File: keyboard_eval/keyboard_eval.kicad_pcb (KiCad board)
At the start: 2 copper layers, 3.4 x 3 mm, 65 parts, among them IC1 IS31FL3733B-TQLS4, J1 Conn_01x03, J2 Conn_01x04, J3 Conn_01x04, J4 Conn_01x07, J5 Conn_01x03, J6 Conn_01x03, J7 Conn_01x06, SW1 RotaryEncoder_Switch

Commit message: WIP layout
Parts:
- added JP4: Jumper_2_Open, Jumper:SolderJumper-2_P1.3mm_Open_RoundedPad1.0x1.5mm, B.Cu at (59.9, 24.1)
- C10, C11, C12, C9, JP1, R5: moved to B.Cu
- JP2, JP3: value Jumper_3_Open -> Jumper_2_Open; footprint Jumper:SolderJumper-3_P1.3mm_Open_RoundedPad1.0x1.5mm -> Jumper:SolderJumper-2_P1.3mm_Open_RoundedPad1.0x1.5mm; moved to B.Cu
- moved R2 193.0 mm to (49.9, 26.2), turned to 180 degrees
- moved C3 192.1 mm to (46.4, 28.2), turned to 180 degrees
- moved C7 190.4 mm to (51.0, 36.5), turned to -90 degrees
- moved C8 185.5 mm to (49.2, 36.5), turned to -90 degrees
- moved C4 185.4 mm to (46.4, 29.9), turned to 180 degrees
- moved R1 176.7 mm to (49.9, 24.2), turned to 180 degrees
- moved R5 175.7 mm to (45.0, 31.4), turned to -90 degrees
- moved R3 175.4 mm to (53.6, 26.2), turned to 180 degrees
- moved JP3 173.9 mm to (46.3, 24.6)
- moved R4 173.0 mm to (56.1, 28.9)
- moved JP2 171.4 mm to (42.6, 24.6)
- moved J3 170.5 mm to (53.2, 21.1), turned to -90 degrees
- moved C6 168.3 mm to (46.4, 33.6), turned to 180 degrees
- moved JP1 167.0 mm to (72.3, 27.7), turned to 90 degrees
- moved C2 165.4 mm to (50.3, 28.1)
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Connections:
- J3 pad 3: Net-(J3-Pad3) -> OLED_SCL
- J3 pad 4: Net-(J3-Pad4) -> OLED_SDA
- JP2 pad 1: OLED_SDA -> LED_SCL
- JP2 pad 2: LED_SDA -> OLED_SDA
- JP3 pad 1: OLED_SCL -> LED_SDA
- JP3 pad 2: LED_SCL -> OLED_SCL
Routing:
- net Col0: track 0.00 -> 102.8 mm, vias 0 -> 7
- net Col2: track 0.00 -> 90.4 mm, vias 0 -> 3
- net Col1: track 0.00 -> 83.0 mm, vias 0 -> 5
- net Row_RE: track 0.00 -> 75.7 mm, vias 0 -> 1
- net Row0: track 0.00 -> 72.8 mm
- net Net-(D11-Pad2): track 0.00 -> 61.4 mm, vias 0 -> 2
- net Net-(D12-Pad2): track 0.00 -> 60.4 mm
- net Row1: track 0.00 -> 53.9 mm
- net Net-(D13-Pad2): track 0.00 -> 53.1 mm
- net Row2_G: track 0.00 -> 51.3 mm, vias 0 -> 4
- net Row2: track 0.00 -> 48.6 mm, vias 0 -> 1
- net Row1_G: track 0.00 -> 44.5 mm, vias 0 -> 4
- net Row0_G: track 0.00 -> 44.2 mm, vias 0 -> 4
- net Row0_R: track 0.00 -> 41.2 mm
- net Row0_B: track 0.00 -> 40.9 mm
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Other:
- board size 3.4 x 3 mm -> 66.5 x 83.5 mm

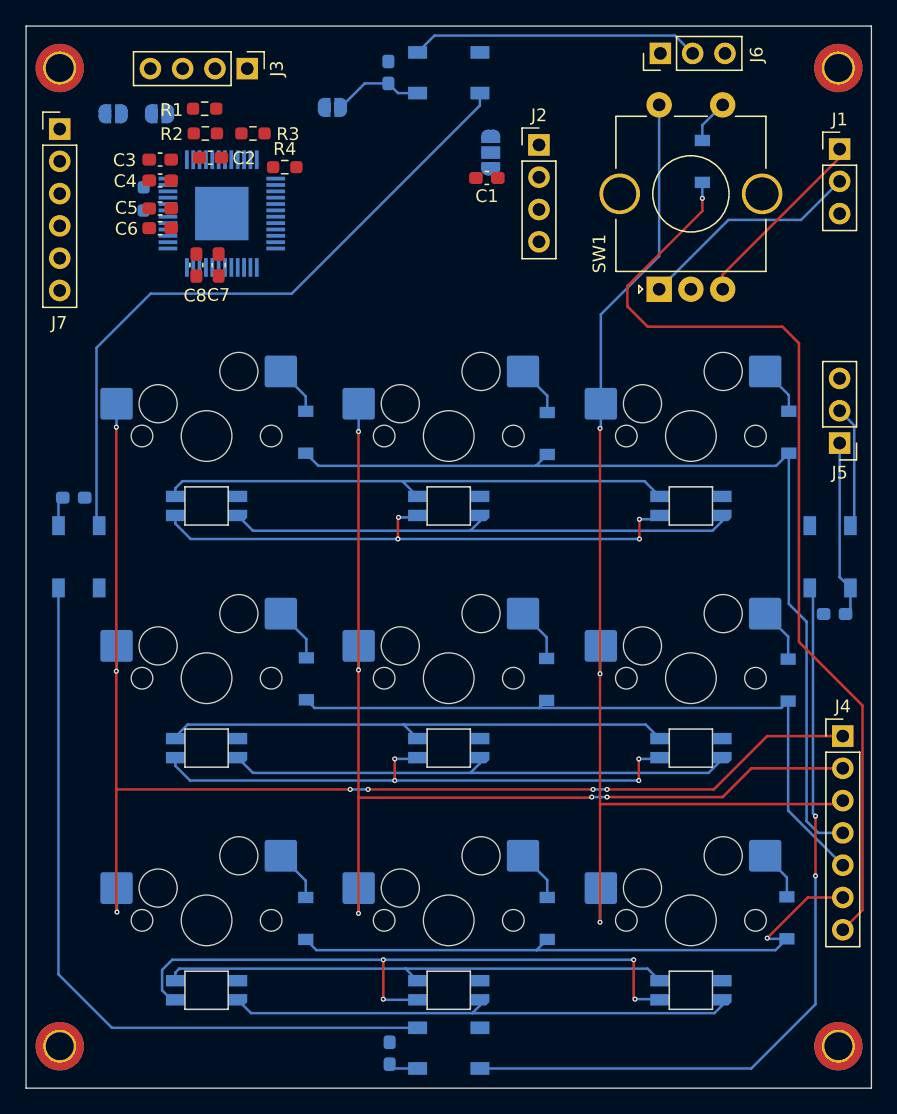
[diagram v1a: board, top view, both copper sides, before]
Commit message: Finished initial layout
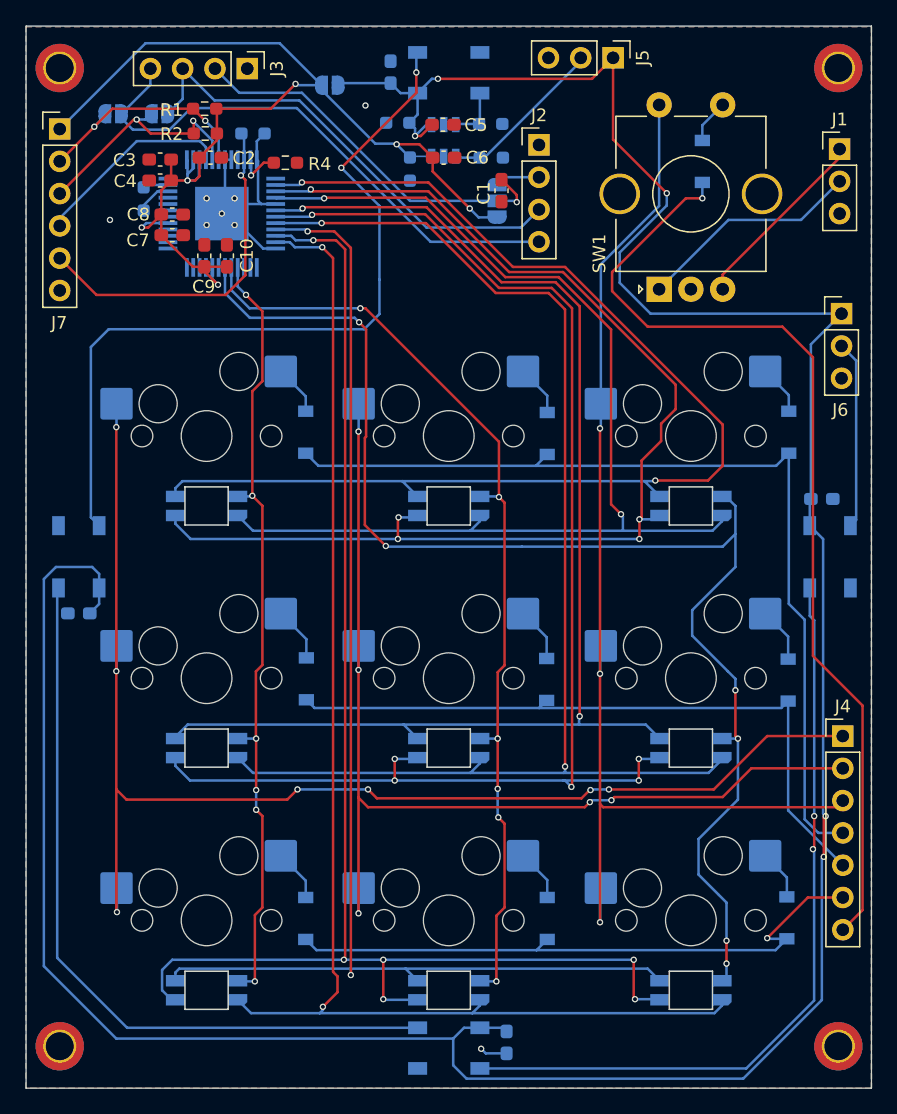
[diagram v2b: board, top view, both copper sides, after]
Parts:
- added C13: 0.1u, Capacitor_SMD:C_0603_1608Metric_Pad1.08x0.95mm_HandSolder, B.Cu at (73.6, 97.7)
- added C14: 0.1u, Capacitor_SMD:C_0603_1608Metric_Pad1.08x0.95mm_HandSolder, B.Cu at (98.4, 55.0)
- added L1: SN74LVC1T45DBVRG4, SamacSys_Parts:SOT95P280X145-6N, B.Cu at (68.7, 26.8)
- added R6: 100k, Resistor_SMD:R_0603_1608Metric_Pad0.98x0.95mm_HandSolder, B.Cu at (65.0, 25.4)
- added R7: 100k, Resistor_SMD:R_0603_1608Metric_Pad0.98x0.95mm_HandSolder, B.Cu at (66.0, 29.0)
- added R8: 100k, Resistor_SMD:R_0603_1608Metric_Pad0.98x0.95mm_HandSolder, B.Cu at (72.3, 25.4)
- added R9: 100k, Resistor_SMD:R_0603_1608Metric_Pad0.98x0.95mm_HandSolder, B.Cu at (72.4, 28.1)
- C10: moved to F.Cu
- C5: value 0.47u -> 0.1u
- C9: value 0.1u -> 0.47u; moved to F.Cu
- R3: moved to B.Cu
- moved C10 64.0 mm to (51.6, 35.8)
- moved C9 57.0 mm to (49.8, 35.8), turned to 90 degrees
- moved C12 49.0 mm to (40.0, 64.0), turned to 180 degrees
- moved D11 48.5 mm to (69.0, 21.4), turned to 0 degrees
- moved D14 48.5 mm to (99.0, 59.5), turned to -90 degrees
- moved D12 48.4 mm to (40.0, 59.5), turned to 90 degrees
- moved D13 48.4 mm to (69.0, 98.2), turned to 180 degrees
- moved C11 41.7 mm to (64.5, 21.4), turned to 90 degrees
- moved J5 35.2 mm to (82.0, 20.2), turned to -90 degrees
- moved J6 24.9 mm to (100.0, 40.4), turned to 0 degrees
- moved C5 23.2 mm to (68.6, 25.5)
- moved C6 23.0 mm to (68.7, 28.1), turned to 0 degrees
- moved C8 4.41 mm to (47.3, 32.6), turned to 0 degrees
- moved C7 4.34 mm to (47.3, 34.2), turned to 0 degrees
- moved JP1 3.83 mm to (72.8, 31.5)
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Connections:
- C10 pad 1: +5V -> VCC
- C5 pad 1: VCC -> GND
- C5 pad 2: GND -> +5V
- C9 pad 1: +5V -> VCC
- D11 pad 4: LED_DIN -> LED_DIN_5V
- J2 pad 2: Net-(C1-Pad1) -> OLED_VCC
- J3 pad 2: OLED_VCC -> Net-(C1-Pad1)
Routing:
- net +5V: track 25.8 -> 237.6 mm, vias 0 -> 5
- net LED_Col2: track 0.00 -> 105.2 mm, vias 0 -> 6
- net VCC: track 0.00 -> 89.6 mm, vias 0 -> 6
- net LED_Col1: track 0.00 -> 75.4 mm, vias 0 -> 6
- net Row2_B: track 40.5 -> 105.7 mm, vias 0 -> 2
- net Row1_G: track 44.5 -> 109.5 mm, vias 4 -> 6
- net Row2_R: track 40.6 -> 104.8 mm, vias 0 -> 2
- net LED_Col0: track 0.00 -> 62.3 mm, vias 0 -> 6
- net Row1_B: track 40.7 -> 102.8 mm, vias 0 -> 2
- net Row2_G: track 51.3 -> 113.2 mm, vias 4 -> 6
- net Row1_R: track 40.6 -> 100.8 mm, vias 0 -> 2
- net Row0_R: track 41.2 -> 94.2 mm, vias 0 -> 2
- net Row0_G: track 44.2 -> 93.9 mm, vias 4 -> 5
- net Row0_B: track 40.9 -> 87.8 mm, vias 0 -> 2
- net OLED_SDA: track 0.00 -> 43.1 mm
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- added copper zone on B.Cu, net GND
- added copper zone on F.Cu, net GND

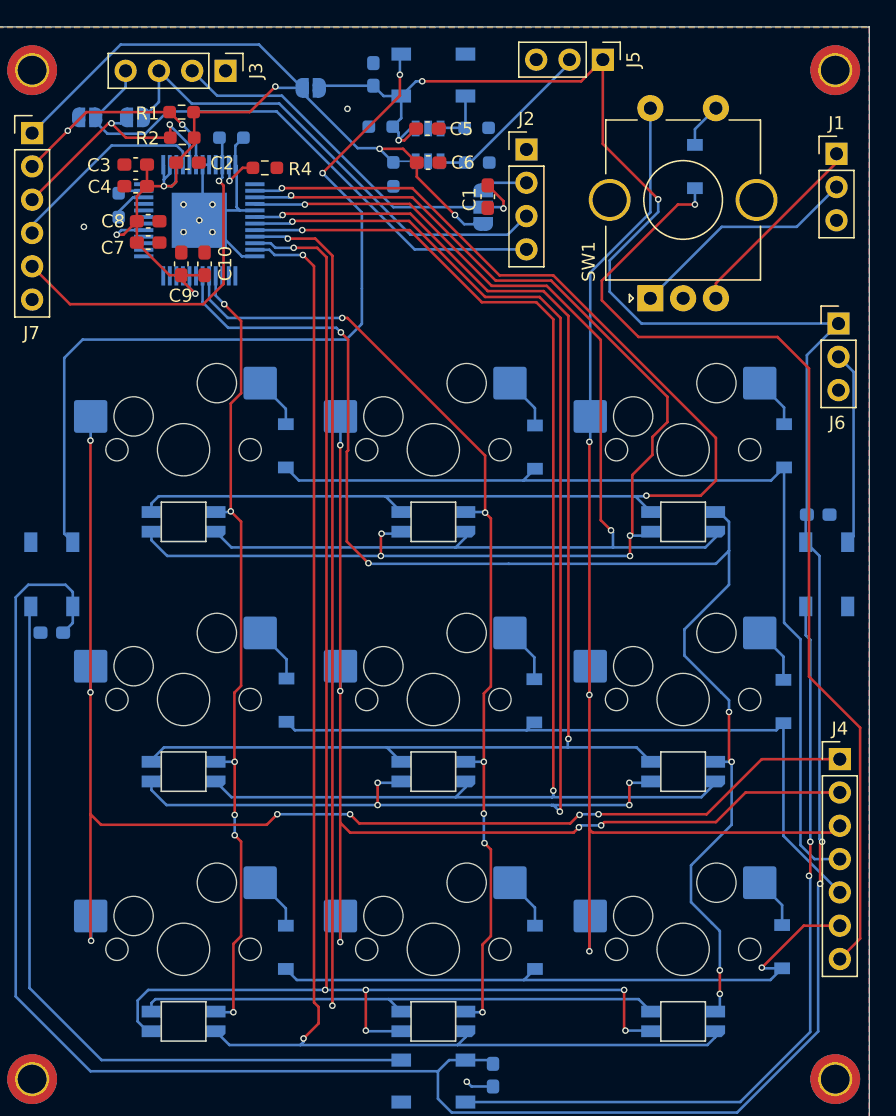
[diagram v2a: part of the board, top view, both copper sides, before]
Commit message: Fixing RGB LED footprint. Fixing missing bits of copper fill
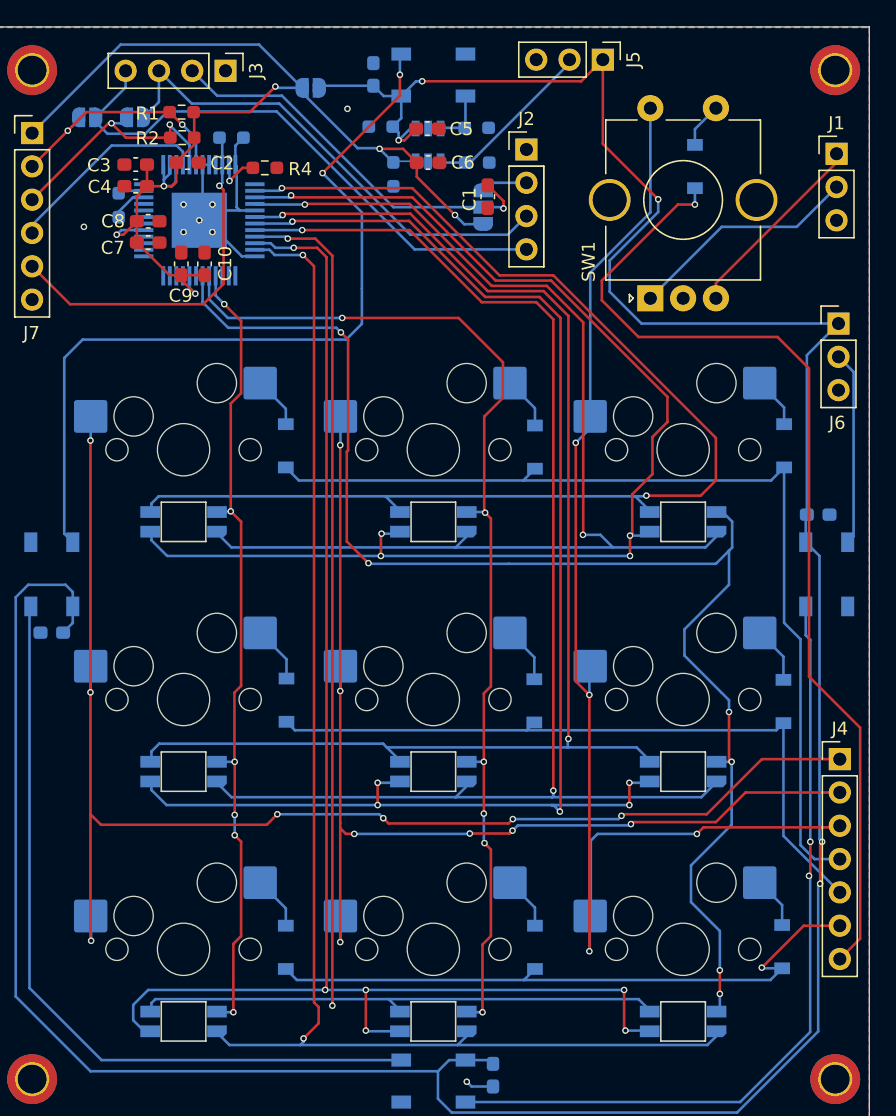
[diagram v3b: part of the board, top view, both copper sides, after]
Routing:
- net Col2: track 90.6 -> 100.0 mm, vias 3 -> 4
- net LED_Col1: track 75.4 -> 81.4 mm
- net Row0_B: track 87.8 -> 88.6 mm
- net Row1_R: track 100.8 -> 101.4 mm
- net Col1: track 83.7 -> 83.6 mm, vias 5 -> 7

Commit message: Adding gerbers and pdf schematic
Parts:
- added G***: LOGO, logo:crisis_boi, F.Cu at (93.0, 97.9)
- added G***: LOGO, logo:logo, B.Cu at (65.6, 36.6)
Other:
- board text added: "Col0"
- board text added: "GND"
- board text added: "Row0"

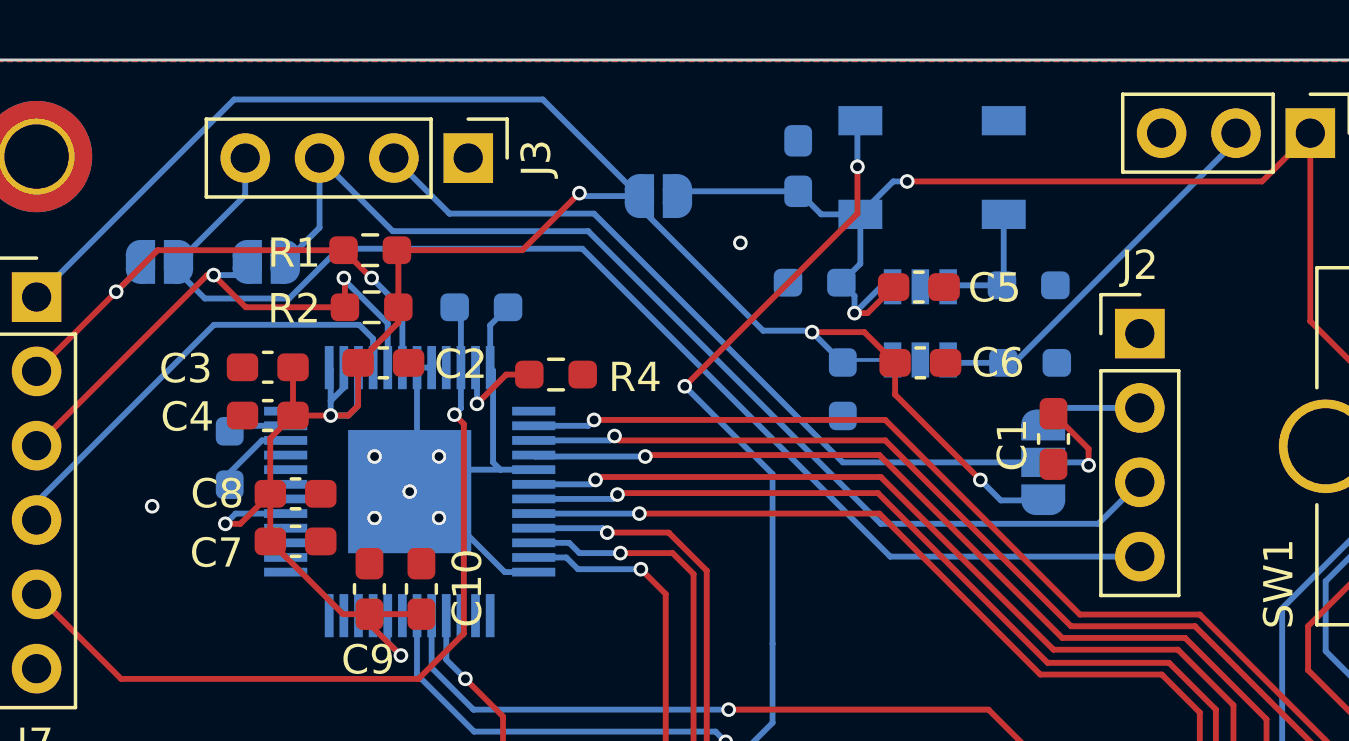
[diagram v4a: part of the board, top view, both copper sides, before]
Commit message: Fixing schematics and firmware
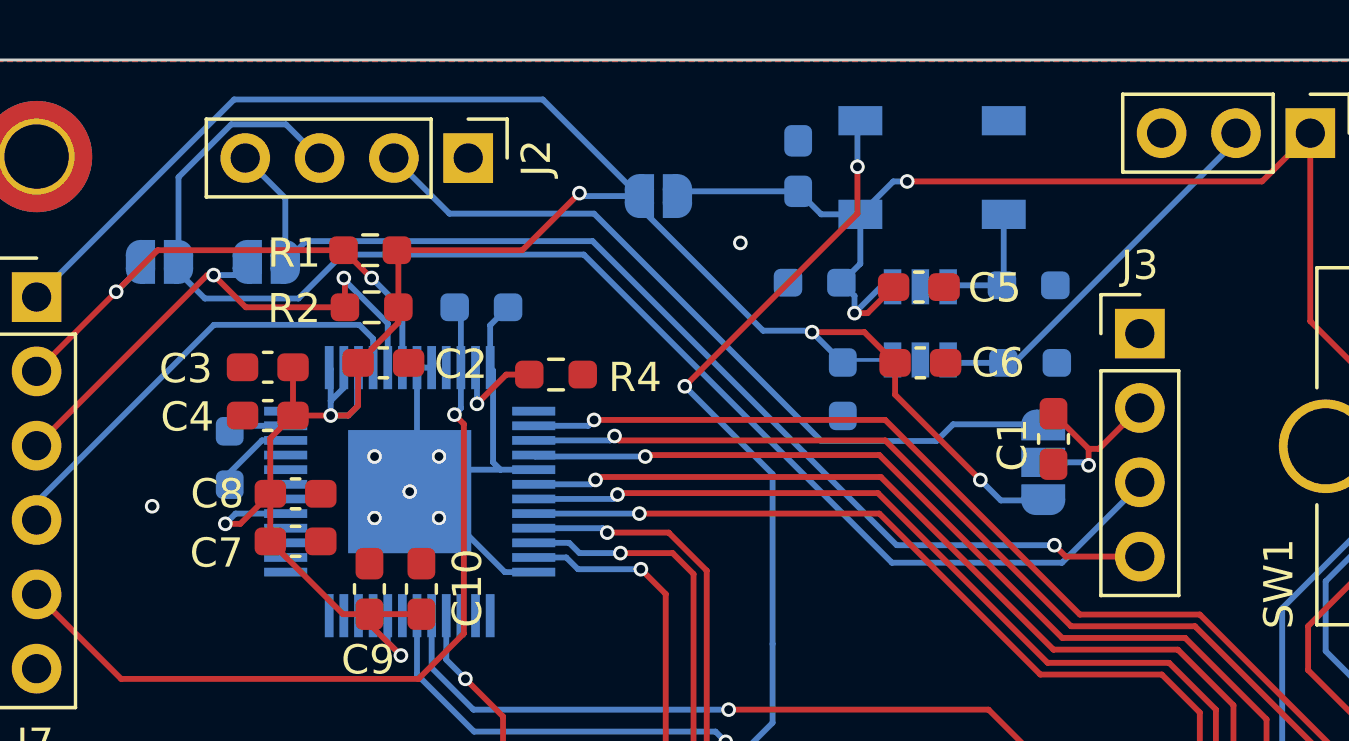
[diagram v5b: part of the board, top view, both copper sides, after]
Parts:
- moved J2 23.7 mm to (53.2, 21.1), turned to -90 degrees
- moved J3 23.7 mm to (76.2, 27.1), turned to 0 degrees
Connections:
- JP2 pad 2: OLED_SDA -> OLED_SCL
- JP3 pad 2: OLED_SCL -> OLED_SDA
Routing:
- net Net-(C1-Pad1): track 30.3 -> 6.18 mm
- net OLED_VCC: track 3.53 -> 26.4 mm
- net OLED_SCL: track 37.8 -> 48.7 mm
- net OLED_SDA: track 43.1 -> 38.1 mm, vias 0 -> 1
